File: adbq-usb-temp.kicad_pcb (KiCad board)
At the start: 4 copper layers, 40.3 x 16 mm, 78 parts, among them J4 USB_C_Receptacle_USB2.0_14P, Q1 Q_NMOS, Q2 Q_NMOS, Q3 Q_NMOS, SW1 SW_Push, SW2 TestPoint, SW3 TestPoint, SW4 TestPoint, U1 ESP32-S3FH4R2, U14 TMP117AIDRV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

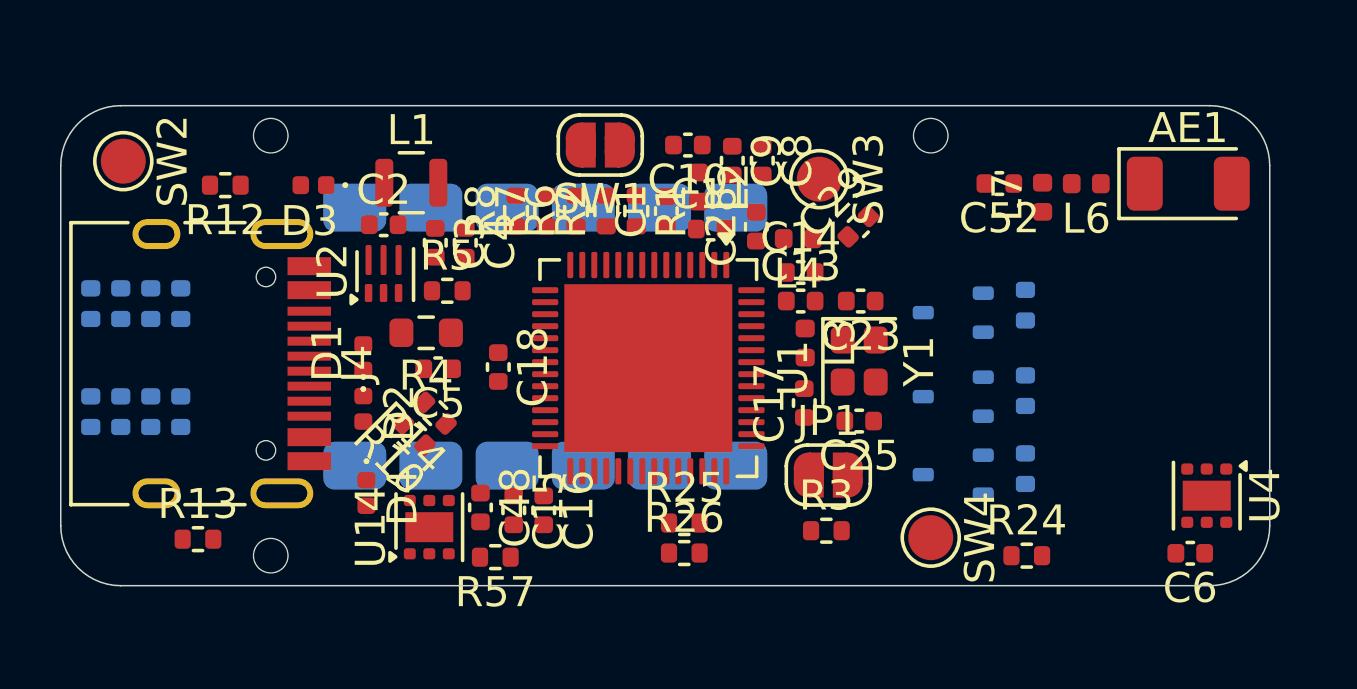
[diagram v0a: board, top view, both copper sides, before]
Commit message: pcb: add fiducials
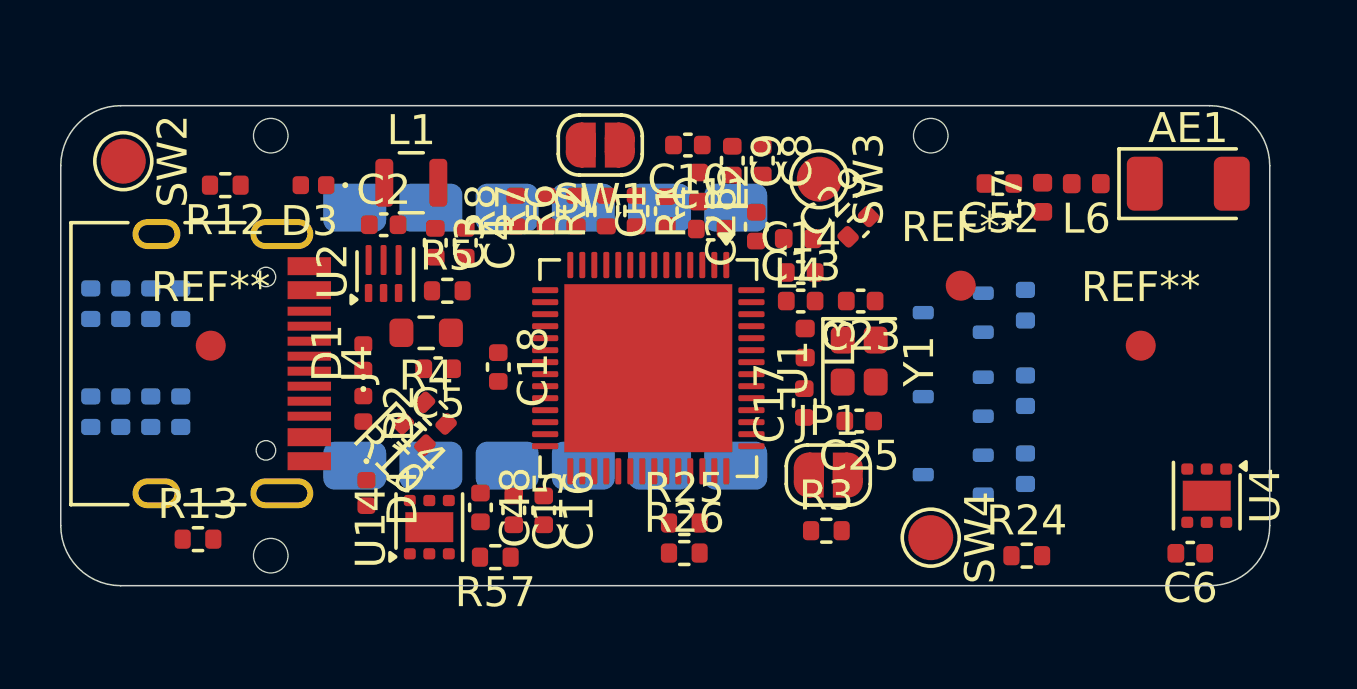
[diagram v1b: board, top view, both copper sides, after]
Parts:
- added REF**: Fiducial_1mm_Mask2mm, Fiducial:Fiducial_1mm_Mask2mm, F.Cu at (118.0, 95.0)
- added REF**: Fiducial_1mm_Mask2mm, Fiducial:Fiducial_1mm_Mask2mm, F.Cu at (87.0, 95.0)
- added REF**: Fiducial_1mm_Mask2mm, Fiducial:Fiducial_1mm_Mask2mm, F.Cu at (112.0, 93.0)

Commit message: pcb: add gnd vias
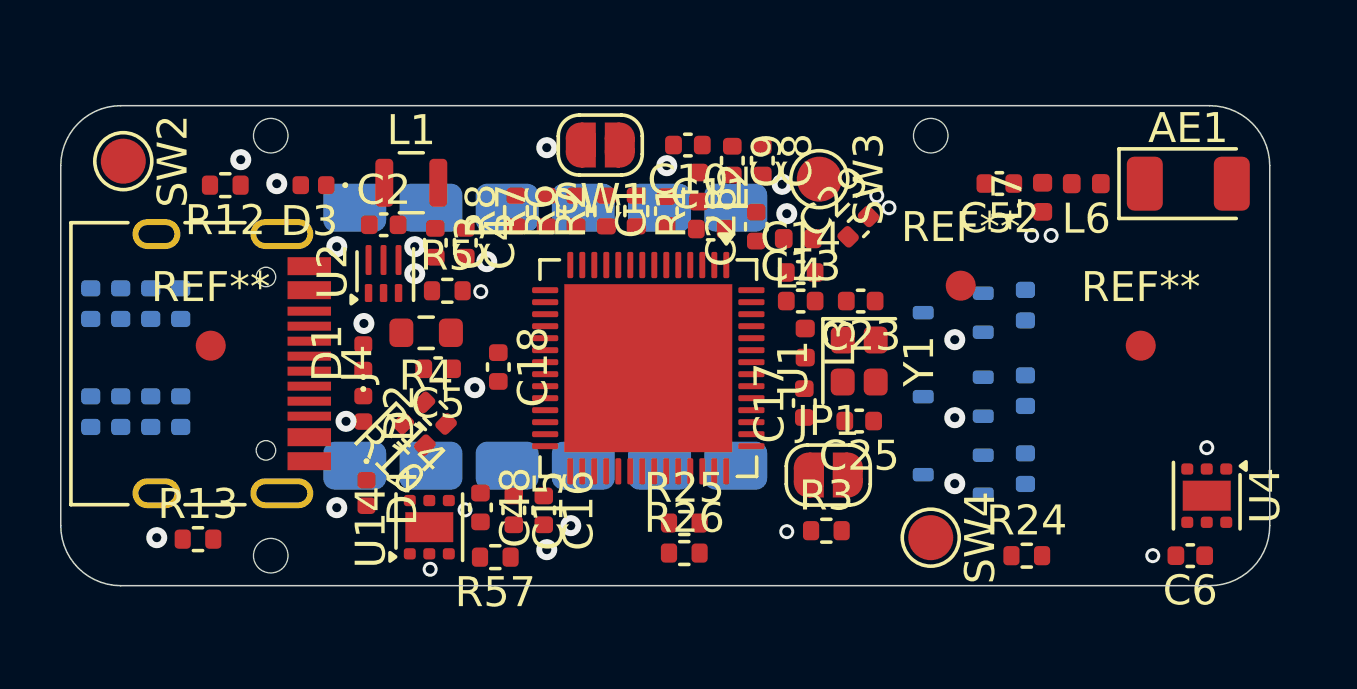
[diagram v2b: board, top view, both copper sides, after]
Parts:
- moved C6 0.08 mm to (119.7, 102.0)
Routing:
- net GND: vias 0 -> 30
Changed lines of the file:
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@@
 	(footprint "Capacitor_SMD:C_0402_1005Metric"
 		(layer "F.Cu")
-		(at 119.65 101.92 180)
+		(at 119.65 102 180)
 		(descr "Capacitor SMD 0402 (1005 Metric), square (rectangular) end terminal, IPC-7351 nominal, (Body size source: IPC-SM-782 page 76, https://www.pcb-3d.com/wordpress/wp-content/uploads/ipc-sm-782a_amendment_1_and_2.pdf), generated with kicad-footprint-generator")
 		(tags "capacitor")
@@
 		(layer "Edge.Cuts")
 	)
+	(via
+		(at 115.012527 91.326119)
+		(size 0.5)
+		(drill 0.3)
+		(layers "F.Cu" "B.Cu")
+		(net 3)
+	)
+	(via
+		(at 109.2 90)
+		(size 0.5)
+		(drill 0.3)
+		(layers "F.Cu" "B.Cu")
+		(net 3)
+	)
+	(via
+		(at 91.2 100.4)
+		(size 0.7)
+		(drill 0.3)
+		(layers "F.Cu" "B.Cu")
+		(free yes)
+		(net 3)
+	)
+	(via
+		(at 99 101)
+		(size 0.7)
+		(drill 0.3)
+		(layers "F.Cu" "B.Cu")
+		(free yes)
+		(net 3)
+	)
+	(via
+		(at 106.2 101.2)
+		(size 0.5)
+		(drill 0.3)
+		(layers "F.Cu" "B.Cu")
+		(net 3)
+	)
+	(via
+		(at 114.363912 91.326119)
+		(size 0.5)
+		(drill 0.3)
+		(layers "F.Cu" "B.Cu")
+		(net 3)
+	)
+	(via
+		(at 96.2 92.2)
+		(size 0.7)
+		(drill 0.3)
+		(layers "F.Cu" "B.Cu")
+		(free yes)
+		(net 3)
+	)
+	(via
+		(at 106.046774 89.621183)
+		(size 0.7)
+		(drill 0.3)
+		(layers "F.Cu" "B.Cu")
+		(free yes)
+		(net 3)
+	)
+	(via
+		(at 111.8 99.6)
+		(size 0.7)
+		(drill 0.3)
+		(layers "F.Cu" "B.Cu")
+		(free yes)
+		(net 3)
+	)
+	(via
+		(at 95.8 96.4)
+		(size 0.7)
+		(drill 0.3)
+		(layers "F.Cu" "B.Cu")
+		(free yes)
+		(net 3)
+	)
+	(via
+		(at 95.477349 100.472141)
+		(size 0.5)
+		(drill 0.3)
+		(layers "F.Cu" "B.Cu")
+		(net 3)
+	)
+	(via
+		(at 89.2 89.6)
+		(size 0.7)
+		(drill 0.3)
+		(layers "F.Cu" "B.Cu")
+		(free yes)
+		(net 3)
+	)
+	(via
+		(at 98.2 101.8)
+		(size 0.7)
+		(drill 0.3)
+		(layers "F.Cu" "B.Cu")
+		(free yes)
+		(net 3)
+	)
+	(via
+		(at 92.105099 94.260056)
+		(size 0.7)
+		(drill 0.3)
+		(layers "F.Cu" "B.Cu")
+		(free yes)
+		(net 3)
+	)
+	(via
+		(at 85.2 101.4)
+		(size 0.7)
+		(drill 0.3)
+		(layers "F.Cu" "B.Cu")
+		(free yes)
+		(net 3)
+	)
+	(via
+		(at 111.8 97.4)
+		(size 0.7)
+		(drill 0.3)
+		(layers "F.Cu" "B.Cu")
+		(free yes)
+		(net 3)
+	)
+	(via
+		(at 96 93.2)
+		(size 0.5)
+		(drill 0.3)
+		(layers "F.Cu" "B.Cu")
+		(net 3)
+	)
+	(via
+		(at 102.2 89)
+		(size 0.7)
+		(drill 0.3)
+		(layers "F.Cu" "B.Cu")
+		(free yes)
+		(net 3)
+	)
+	(via
+		(at 93.8 91.7)
+		(size 0.7)
+		(drill 0.3)
+		(layers "F.Cu" "B.Cu")
+		(free yes)
+		(net 3)
+	)
+	(via
+		(at 109.608075 90.402691)
+		(size 0.5)
+		(drill 0.3)
+		(layers "F.Cu" "B.Cu")
+		(net 3)
+	)
+	(via
+		(at 94.313175 102.453118)
+		(size 0.5)
+		(drill 0.3)
+		(layers "F.Cu" "B.Cu")
+		(net 3)
+	)
+	(via
+		(at 111.8 94.8)
+		(size 0.7)
+		(drill 0.3)
+		(layers "F.Cu" "B.Cu")
+		(free yes)
+		(net 3)
+	)
+	(via
+		(at 98.2 88.4)
+		(size 0.7)
+		(drill 0.3)
+		(layers "F.Cu" "B.Cu")
+		(free yes)
+		(net 3)
+	)
+	(via
+		(at 93.8 92.6)
+		(size 0.7)
+		(drill 0.3)
+		(layers "F.Cu" "B.Cu")
+		(free yes)
+		(net 3)
+	)
+	(via
+		(at 88 88.8)
+		(size 0.7)
+		(drill 0.3)
+		(layers "F.Cu" "B.Cu")
+		(free yes)
+		(net 3)
+	)
+	(via
+		(at 91.2 91.7)
+		(size 0.7)
+		(drill 0.3)
+		(layers "F.Cu" "B.Cu")
+		(free yes)
+		(net 3)
+	)
+	(via
+		(at 120.2 98.4)
+		(size 0.5)
+		(drill 0.3)
+		(layers "F.Cu" "B.Cu")
+		(net 3)
+	)
+	(via
+		(at 118.4 102)
+		(size 0.5)
+		(drill 0.3)
+		(layers "F.Cu" "B.Cu")
+		(net 3)
+	)
+	(via
+		(at 91.509517 97.522009)
+		(size 0.7)
+		(drill 0.3)
+		(layers "F.Cu" "B.Cu")
+		(free yes)
+		(net 3)
+	)
+	(via
+		(at 106.2 90.6)
+		(size 0.7)
+		(drill 0.3)
+		(layers "F.Cu" "B.Cu")
+		(free yes)
+		(net 3)
+	)
 	(zone

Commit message: pcb: add rf routing
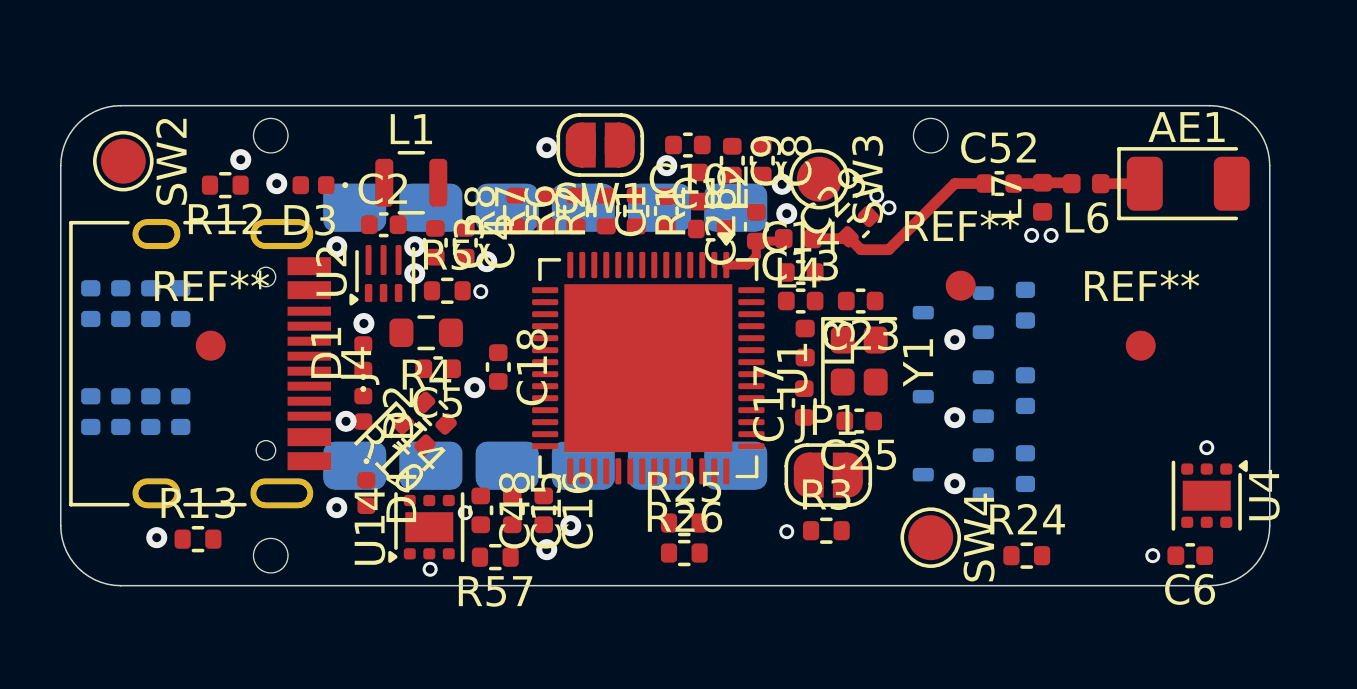
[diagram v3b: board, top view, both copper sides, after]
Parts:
- moved C48 0.10 mm to (96.0, 100.5)
- moved C15 0.05 mm to (97.1, 100.5)
- turned C52 to 0 degrees
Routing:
- net /RF_TRANS: track 0.00 -> 6.85 mm
- net /RF_ESP: track 0.00 -> 2.57 mm
- net Net-(C52-Pad2): track 0.00 -> 1.96 mm
- net /RF_ANT: track 0.00 -> 1.47 mm
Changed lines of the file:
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@@
 	(footprint "Capacitor_SMD:C_0402_1005Metric"
 		(layer "F.Cu")
-		(at 95.99 100.3925 -90)
+		(at 96 100.489118 -90)
 		(descr "Capacitor SMD 0402 (1005 Metric), square (rectangular) end terminal, IPC-7351 nominal, (Body size source: IPC-SM-782 page 76, https://www.pcb-3d.com/wordpress/wp-content/uploads/ipc-sm-782a_amendment_1_and_2.pdf), generated with kicad-footprint-generator")
 		(tags "capacitor")
@@
 	(footprint "Capacitor_SMD:C_0402_1005Metric"
 		(layer "F.Cu")
-		(at 113.286546 89.595175 180)
+		(at 113.286546 89.595175)
 		(descr "Capacitor SMD 0402 (1005 Metric), square (rectangular) end terminal, IPC-7351 nominal, (Body size source: IPC-SM-782 page 76, https://www.pcb-3d.com/wordpress/wp-content/uploads/ipc-sm-782a_amendment_1_and_2.pdf), generated with kicad-footprint-generator")
 		(tags "capacitor")
@@
 		)
 		(property "Manufacturer" "Guangdong Fenghua Advanced Tech (FH)"
-			(at 0 0 180)
+			(at 0 0 0)
 			(unlocked yes)
 			(layer "F.Fab")
@@
 		)
 		(property "Manufacturer Part Number" "0402CG1R0C500NT"
-			(at 0 0 180)
+			(at 0 0 0)
 			(unlocked yes)
 			(layer "F.Fab")
@@
 		)
 		(property "Basic" "X"
-			(at 0 0 180)
+			(at 0 0 0)
 			(unlocked yes)
 			(layer "F.Fab")
@@
 		)
 		(property "JLCPCB Part #" "C1550"
-			(at 0 0 180)
+			(at 0 0 0)
 			(unlocked yes)
 			(layer "F.Fab")
@@
 		(attr smd)
 		(fp_line
-			(start -0.107836 0.36)
-			(end 0.107836 0.36)
+			(start -0.107836 -0.36)
+			(end 0.107836 -0.36)
 			(stroke
 				(width 0.12)
@@
 		)
 		(fp_line
-			(start -0.107836 -0.36)
-			(end 0.107836 -0.36)
+			(start -0.107836 0.36)
+			(end 0.107836 0.36)
 			(stroke
 				(width 0.12)
@@
 		)
 		(fp_line
-			(start 0.91 0.46)
-			(end -0.91 0.46)
+			(start -0.91 -0.46)
+			(end 0.91 -0.46)
 			(stroke
 				(width 0.05)
@@
 		)
 		(fp_line
-			(start 0.91 -0.46)
-			(end 0.91 0.46)
+			(start -0.91 0.46)
+			(end -0.91 -0.46)
 			(stroke
 				(width 0.05)
@@
 		)
 		(fp_line
-			(start -0.91 0.46)
-			(end -0.91 -0.46)
+			(start 0.91 -0.46)
+			(end 0.91 0.46)
 			(stroke
 				(width 0.05)
@@
 		)
 		(fp_line
-			(start -0.91 -0.46)
-			(end 0.91 -0.46)
+			(start 0.91 0.46)
+			(end -0.91 0.46)
 			(stroke
 				(width 0.05)
@@
 		)
 		(fp_line
-			(start 0.5 0.25)
-			(end -0.5 0.25)
+			(start -0.5 -0.25)
+			(end 0.5 -0.25)
 			(stroke
 				(width 0.1)
@@
 		)
 		(fp_line
-			(start 0.5 -0.25)
-			(end 0.5 0.25)
+			(start -0.5 0.25)
+			(end -0.5 -0.25)
 			(stroke
 				(width 0.1)
@@
 		)
 		(fp_line
-			(start -0.5 0.25)
-			(end -0.5 -0.25)
+			(start 0.5 -0.25)
+			(end 0.5 0.25)
 			(stroke
 				(width 0.1)
@@
 		)
 		(fp_line
-			(start -0.5 -0.25)
-			(end 0.5 -0.25)
+			(start 0.5 0.25)
+			(end -0.5 0.25)
 			(stroke
 				(width 0.1)
@@
 		)
 		(pad "1" smd roundrect
-			(at -0.48 0 180)
+			(at -0.48 0)
 			(size 0.56 0.62)
 			(layers "F.Cu" "F.Mask" "F.Paste")
@@
 		)
 		(pad "2" smd roundrect
-			(at 0.48 0 180)
+			(at 0.48 0)
 			(size 0.56 0.62)
 			(layers "F.Cu" "F.Mask" "F.Paste")
@@
 		(zone_connect 1)
 		(attr exclude_from_pos_files exclude_from_bom allow_soldermask_bridges)
-		(fp_rect
-			(start -0.15 -0.75)
-			(end 0.15 0.75)
-			(stroke
-				(width 0)
-				(type default)
-			)
-			(fill yes)
-			(layer "F.Mask")
-		)
 		(fp_line
 			(start -1.4 0.3)
@@
 		(zone_connect 1)
 		(attr exclude_from_pos_files exclude_from_bom allow_soldermask_bridges)
-		(fp_rect
-			(start -0.15 -0.75)
-			(end 0.15 0.75)
-			(stroke
-				(width 0)
-				(type default)
-			)
-			(fill yes)
-			(layer "F.Mask")
-		)
 		(fp_line
 			(start 1.4 -0.3)
@@
 	(footprint "Capacitor_SMD:C_0402_1005Metric"
 		(layer "F.Cu")
-		(at 97.100247 100.489118 -90)
+		(at 97.050124 100.489118 -90)
 		(descr "Capacitor SMD 0402 (1005 Metric), square (rectangular) end terminal, IPC-7351 nominal, (Body size source: IPC-SM-782 page 76, https://www.pcb-3d.com/wordpress/wp-content/uploads/ipc-sm-782a_amendment_1_and_2.pdf), generated with kicad-footprint-generator")
 		(tags "capacitor")
@@
 		(layer "Edge.Cuts")
 	)
+	(segment
+		(start 116.67 89.6)
+		(end 118.135 89.6)
+		(width 0.359)
+		(layer "F.Cu")
+		(net 1)
+	)
 	(via
 		(at 115.012527 91.326119)
@@
 	)
 	(via
-		(at 95.477349 100.472141)
+		(at 95.484999 100.566963)
 		(size 0.5)
 		(drill 0.3)
@@
 		(net 3)
 	)
+	(segment
+		(start 105.185 92.015)
+		(end 105.185 91.5125)
+		(width 0.3)
+		(layer "F.Cu")
+		(net 11)
+	)
+	(segment
+		(start 106.02 91.5125)
+		(end 106.1 91.4325)
+		(width 0.3)
+		(layer "F.Cu")
+		(net 11)
+	)
+	(segment
+		(start 104.8875 92.3125)
+		(end 105.185 92.015)
+		(width 0.3)
+		(layer "F.Cu")
+		(net 11)
+	)
+	(segment
+		(start 105.185 91.5125)
+		(end 106.02 91.5125)
+		(width 0.3)
+		(layer "F.Cu")
+		(net 11)
+	)
+	(segment
+		(start 104.185 92.3125)
+		(end 104.8875 92.3125)
+		(width 0.3)
+		(layer "F.Cu")
+		(net 11)
+	)
+	(segment
+		(start 109.6 91.8)
+		(end 111.804825 89.595175)
+		(width 0.359)
+		(layer "F.Cu")
+		(net 12)
+	)
+	(segment
+		(start 108.245589 91.371911)
+		(end 108.673678 91.8)
+		(width 0.359)
+		(layer "F.Cu")
+		(net 12)
+	)
+	(segment
+		(start 108.185 91.4325)
+		(end 107.07 91.4325)
+		(width 0.359)
+		(layer "F.Cu")
+		(net 12)
+	)
+	(segment
+		(start 108.673678 91.8)
+		(end 109.6 91.8)
+		(width 0.359)
+		(layer "F.Cu")
+		(net 12)
+	)
+	(segment
+		(start 108.245589 91.371911)
+		(end 108.185 91.4325)
+		(width 0.359)
+		(layer "F.Cu")
+		(net 12)
+	)
+	(segment
+		(start 111.804825 89.595175)
+		(end 112.806546 89.595175)
+		(width 0.359)
+		(layer "F.Cu")
+		(net 12)
+	)
+	(segment
+		(start 115.66961 89.56961)
+		(end 115.7 89.6)
+		(width 0.359)
+		(layer "F.Cu")
+		(net 13)
+	)
+	(segment
+		(start 113.766546 89.595175)
+		(end 114.702346 89.595175)
+		(width 0.359)
+		(layer "F.Cu")
+		(net 13)
+	)
+	(segment
+		(start 114.727911 89.56961)
+		(end 115.66961 89.56961)
+		(width 0.359)
+		(layer "F.Cu")
+		(net 13)
+	)
+	(segment
+		(start 114.702346 89.595175)
+		(end 114.727911 89.56961)
+		(width 0.359)
+		(layer "F.Cu")
+		(net 13)
+	)
 	(zone

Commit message: pcb: add HSE routing
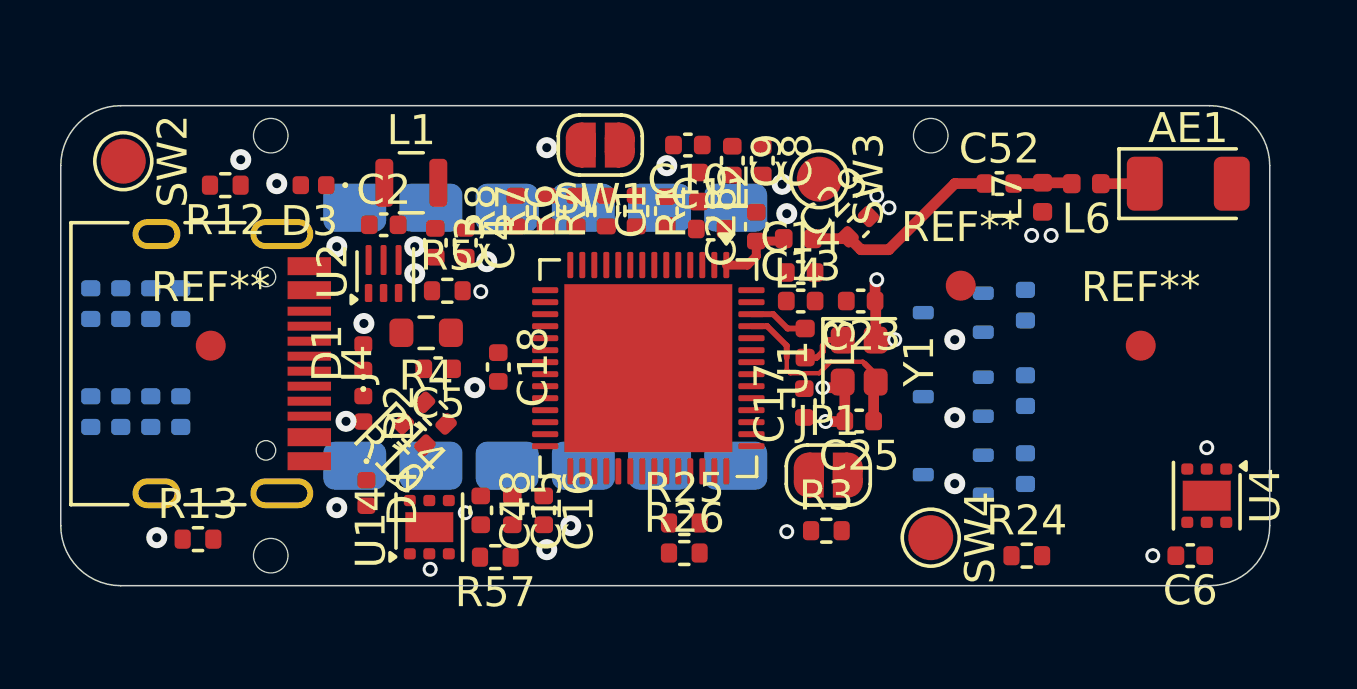
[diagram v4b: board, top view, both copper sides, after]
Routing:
- net /XTAL_N: track 0.00 -> 7.17 mm
- net GND: track 0.00 -> 5.67 mm, vias 30 -> 34
- net /XTAL_P: track 0.00 -> 1.99 mm
- net /XTAL_PL: track 0.00 -> 1.61 mm

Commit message: pcb: add USB routing
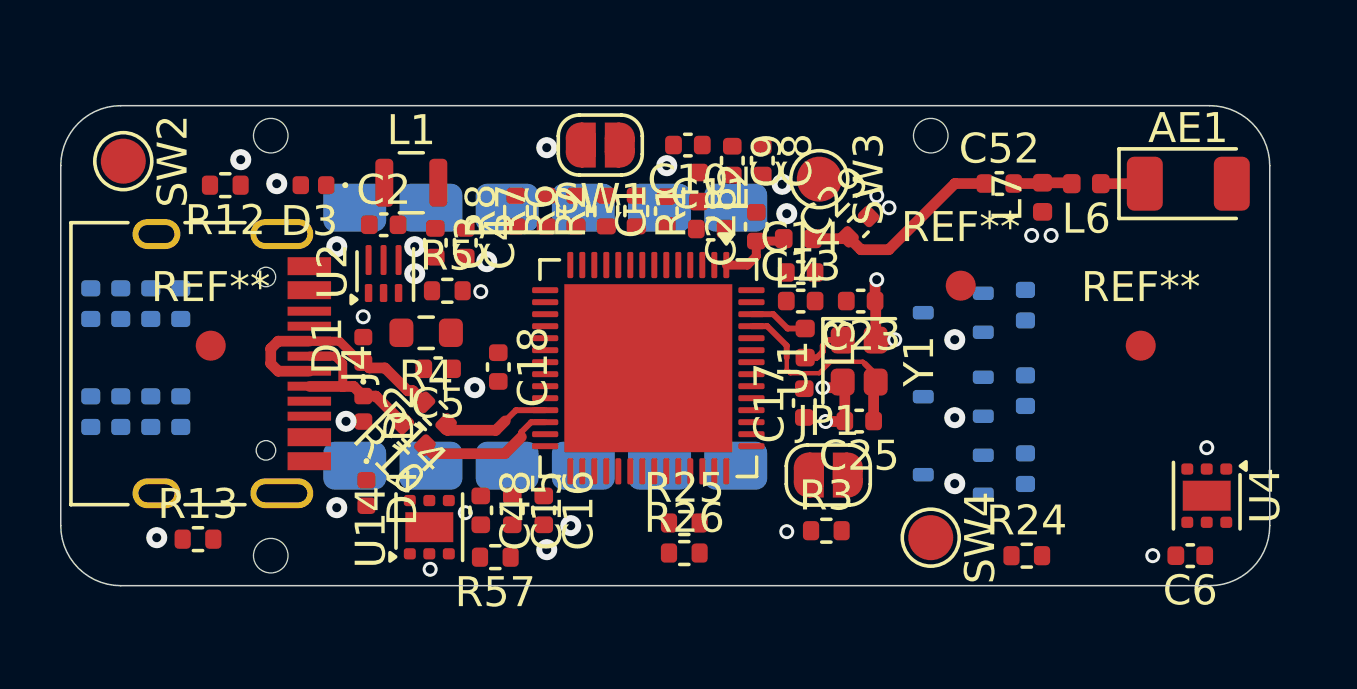
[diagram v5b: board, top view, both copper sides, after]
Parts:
- moved D1 0.24 mm to (92.1, 95.2)
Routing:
- net /D-: track 0.00 -> 7.96 mm
- net /D+: track 0.00 -> 5.61 mm
- net /ESP_D+: track 0.00 -> 4.67 mm
- net /ESP_D-: track 0.00 -> 3.77 mm
